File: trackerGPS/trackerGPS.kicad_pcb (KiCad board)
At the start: 4 copper layers, 89.4 x 33.6 mm, 47 parts, among them IC1 PIC32MM0256GPM028-I_ML, IC4 MAX17263LETD+, IC5 L86-M33, J1 USB_A, J2 Conn, J3 902-9235, Q1 BC847BW,115, Q2 BC847BW,115, U1 REG113NA-3.3_3K, U2 1043P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

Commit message: modified:   trackerGPS/microcontroller.bak 	modified:   trackerGPS/powerSupply.bak 	modified:   trackerGPS/powerSupply.sch 	modified:   trackerGPS/trackerGPS-cache.lib 	modified:   trackerGPS/trackerGPS.bak 	modified:   trackerGPS/trackerGPS.kicad_pcb 	modified:   trackerGPS/trackerGPS.kicad_pcb-bak
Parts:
- removed IC4: MAX17263LETD+, MAX17263LETD+:SON40P300X300X80-15N
- added IC2: BQ24072TRGTT, Package_DFN_QFN:QFN-16-1EP_3x3mm_P0.5mm_EP2.7x2.7mm_ThermalVias, F.Cu at (162.9, 91.8)
- added J4: USB_A, USB_JAE:DX4R005HJ5, F.Cu at (149.6, 106.9)
- moved C13 5.15 mm to (199.1, 34.8)
- moved C25 5.15 mm to (204.1, 40.9)
- moved C26 5.15 mm to (212.0, 39.7)
- moved IC1 5.15 mm to (206.2, 33.3)
- moved R7 5.15 mm to (196.6, 48.3)
- moved C10 5.15 mm to (213.2, 35.3)
- moved C12 5.15 mm to (211.1, 35.3)
- moved C22 5.15 mm to (208.3, 28.5)
- moved Q1 5.15 mm to (199.5, 47.8)
- moved Y1 5.15 mm to (208.1, 39.6)
- moved C14 5.15 mm to (201.1, 34.8)
- moved R6 5.15 mm to (199.6, 45.2)

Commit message: added battery charger BQ24072T 	modified:   trackerGPS/powerSupply.bak 	modified:   trackerGPS/powerSupply.sch 	modified:   trackerGPS/sym-lib-table 	modified:   trackerGPS/trackerGPS-cache.lib 	new file:   trackerGPS/trackerGPS-rescue.dcm 	new file:   trackerGPS/trackerGPS-rescue.lib 	modified:   trackerGPS/trackerGPS.kicad_pcb 	modified:   trackerGPS/trackerGPS.kicad_pcb-bak
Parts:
- removed U2: 1043P, 1043P:1043P
- added TP1: TestPoint, TestPoint:TestPoint_Pad_2.0x2.0mm, F.Cu at (181.5, 92.8)
- added TP2: TestPoint, TestPoint:TestPoint_Pad_2.0x2.0mm, F.Cu at (177.7, 92.8)

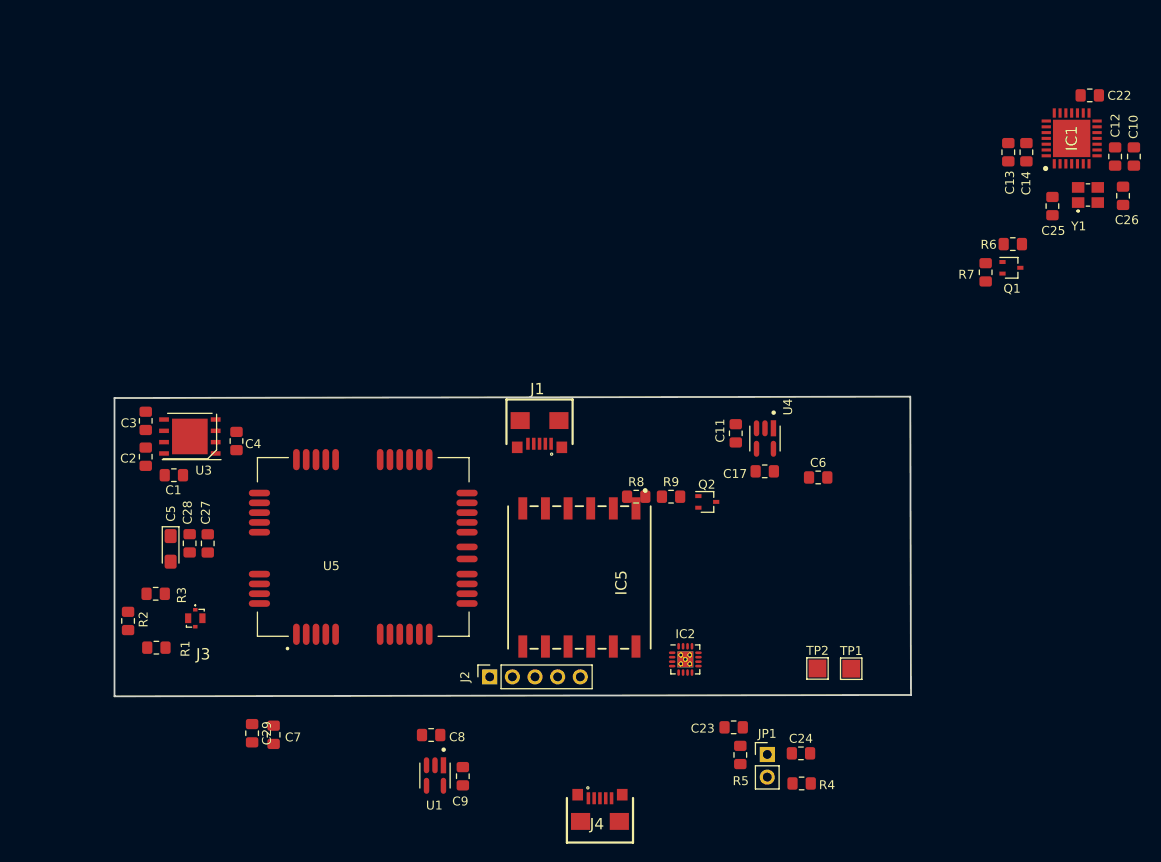
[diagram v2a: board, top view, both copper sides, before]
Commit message: Component placed 	modified:   trackerGPS/microcontroller.bak 	modified:   trackerGPS/microcontroller.sch 	modified:   trackerGPS/powerSupply.bak 	modified:   trackerGPS/powerSupply.sch 	modified:   trackerGPS/simModule.bak 	modified:   trackerGPS/simModule.sch 	modified:   trackerGPS/trackerGPS-cache.lib 	modified:   trackerGPS/trackerGPS.bak 	modified:   trackerGPS/trackerGPS.kicad_pcb 	modified:   trackerGPS/trackerGPS.kicad_pcb-bak 	modified:   trackerGPS/trackerGPS.sch
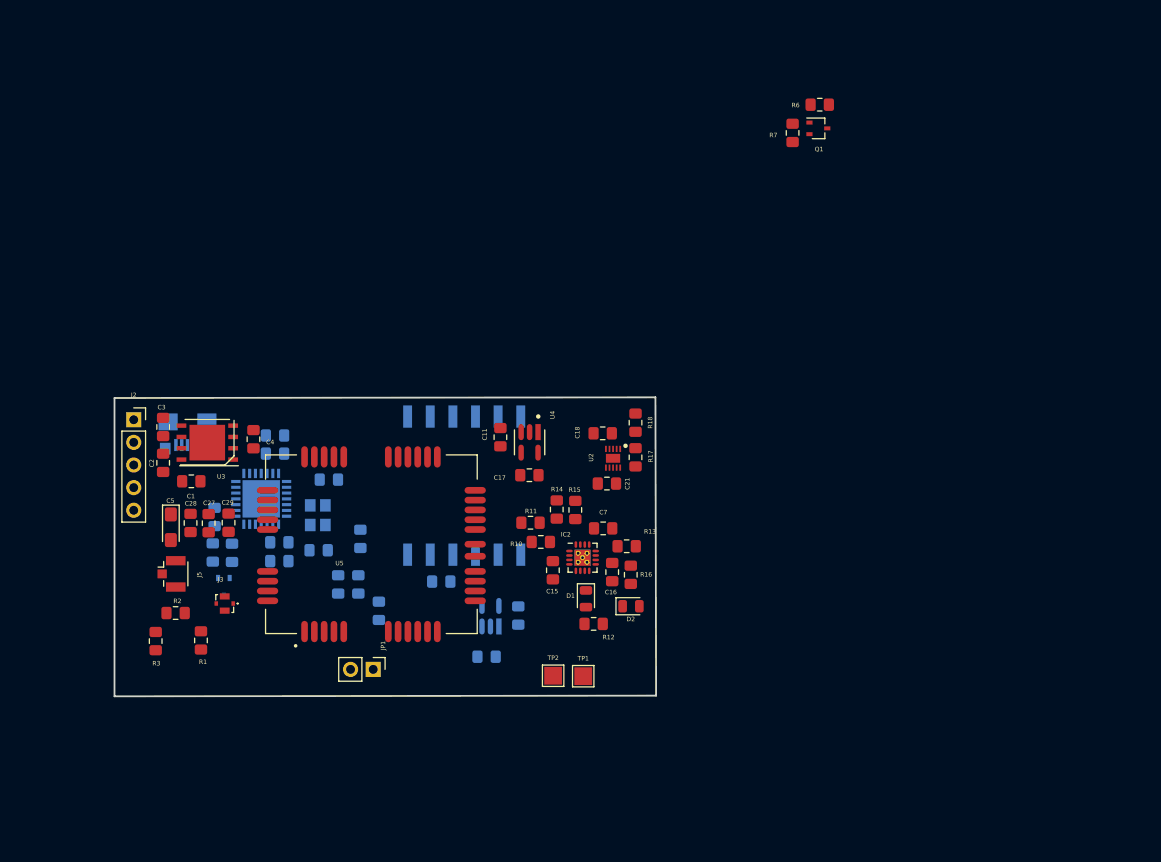
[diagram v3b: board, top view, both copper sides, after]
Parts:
- removed J1: USB_A, USB_JAE:DX4R005HJ5
- added C15: 4.7uF, Capacitor_SMD:C_0805_2012Metric_Pad1.15x1.40mm_HandSolder, F.Cu at (148.0, 81.8)
- added C16: 4.7uF, Capacitor_SMD:C_0805_2012Metric_Pad1.15x1.40mm_HandSolder, F.Cu at (154.7, 82.0)
- added C18: 470nF, Capacitor_SMD:C_0805_2012Metric_Pad1.15x1.40mm_HandSolder, F.Cu at (153.6, 66.4)
- added C21: 10uF, Capacitor_SMD:C_0805_2012Metric_Pad1.15x1.40mm_HandSolder, F.Cu at (154.1, 72.0)
- added D1: LED_Small, LED_SMD:LED_0805_2012Metric, F.Cu at (151.7, 85.0)
- added D2: LED_Small, LED_SMD:LED_0805_2012Metric, F.Cu at (156.8, 85.8)
- added J5: Conn_Coaxial, Connector_Coaxial:U.FL_Hirose_U.FL-R-SMT-1_Vertical, F.Cu at (105.2, 82.2)
- added R10: 200kOhm, Resistor_SMD:R_0805_2012Metric_Pad1.15x1.40mm_HandSolder, F.Cu at (146.7, 78.6)
- added R11: 49.9kOhm, Resistor_SMD:R_0805_2012Metric_Pad1.15x1.40mm_HandSolder, F.Cu at (145.5, 76.4)
- added R12: 1.5kOhm, Resistor_SMD:R_0805_2012Metric_Pad1.15x1.40mm_HandSolder, F.Cu at (152.6, 87.8)
- added R13: NP, Resistor_SMD:R_0805_2012Metric_Pad1.15x1.40mm_HandSolder, F.Cu at (156.3, 79.1)
- added R14: 900ohm, Resistor_SMD:R_0805_2012Metric_Pad1.15x1.40mm_HandSolder, F.Cu at (148.4, 74.9)
- added R15: 0ohm, Resistor_SMD:R_0805_2012Metric_Pad1.15x1.40mm_HandSolder, F.Cu at (150.5, 75.0)
- added R16: 1.5kOhm, Resistor_SMD:R_0805_2012Metric_Pad1.15x1.40mm_HandSolder, F.Cu at (156.7, 82.3)
- added R17: 5.56kOhm, Resistor_SMD:R_0805_2012Metric_Pad1.15x1.40mm_HandSolder, F.Cu at (157.3, 69.1)
- added R18: 1kOhm, Resistor_SMD:R_0805_2012Metric_Pad1.15x1.40mm_HandSolder, F.Cu at (157.3, 65.2)
- added U2: TLV75201PDSQT, TLV75201PDSQT:SON40P200X200X80-11N, F.Cu at (154.8, 69.2)
- C10, C12, C13, C14, C22, C23, C24, C25, C26, C6, C8, C9, IC1, IC5, J4, Q2, R4, R5, R8, R9, U1, Y1: moved to B.Cu
- C7: value C_Small -> 1uF
- TP1: value TestPoint -> Battery_GND
- TP2: value TestPoint -> Battery+
- moved C22 109.0 mm to (110.0, 75.8), turned to 270 degrees
- moved C10 106.1 mm to (117.3, 80.7), turned to 0 degrees
- moved C12 103.3 mm to (117.3, 78.6), turned to 0 degrees
- moved IC1 99.5 mm to (115.3, 73.8), turned to 180 degrees
- moved C26 98.6 mm to (121.7, 79.5), turned to 0 degrees
- moved Y1 93.6 mm to (121.6, 75.6), turned to 270 degrees
- moved C14 90.9 mm to (116.8, 68.7), turned to 0 degrees
- moved C13 88.2 mm to (116.8, 66.6), turned to 0 degrees
- moved C25 86.8 mm to (122.9, 71.6), turned to 0 degrees
- moved J4 60.4 mm to (103.3, 68.1)
- moved Q2 55.1 mm to (111.1, 83.6), turned to 270 degrees
- moved R4 54.5 mm to (126.2, 83.4), turned to 90 degrees
- moved R9 51.8 mm to (109.8, 79.8), turned to 90 degrees
- moved C24 50.0 mm to (128.5, 86.3), turned to 90 degrees
- moved J2 49.3 mm to (101.0, 64.9), turned to 0 degrees
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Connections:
- C10 pad 1: /powerSupply/Vcc_3.8V -> /powerSupply/Vcc_3.5V
- C11 pad 1: Net-(C11-Pad1) -> /microcontroller/VBUS
- C12 pad 1: /powerSupply/Vcc_3.8V -> /powerSupply/Vcc_3.5V
- C13 pad 1: /powerSupply/Vcc_3.8V -> /powerSupply/Vcc_3.5V
- C14 pad 1: /powerSupply/Vcc_3.8V -> /powerSupply/Vcc_3.5V
- C23 pad 1: /powerSupply/Vcc_3.8V -> /powerSupply/Vcc_3.5V
- C27 pad 1: /powerSupply/Vcc_3.8V -> /powerSupply/Vcc_3.5V
- C28 pad 1: /powerSupply/Vcc_3.8V -> /powerSupply/Vcc_3.5V
- C29 pad 1: /powerSupply/Vcc_3.8V -> /powerSupply/Vcc_3.5V
- C5 pad 1: /powerSupply/Vcc_3.8V -> /powerSupply/Vcc_3.5V
- C7 pad 1: /powerSupply/Vcc_3.8V -> /microcontroller/VBUS
- C8 pad 1: /powerSupply/Vcc_3.8V -> /powerSupply/3.8V_Bat_5V_USB
- IC1 pad 10: /powerSupply/Vcc_3.8V -> /powerSupply/Vcc_3.5V
- IC1 pad 12: Net-(C11-Pad1) -> /microcontroller/VBUS
- IC1 pad 18: /microcontroller/D- -> /microcontroller/USB-
- IC1 pad 19: /microcontroller/D+ -> /microcontroller/USB+
- IC1 pad 25: /powerSupply/Vcc_3.8V -> /powerSupply/Vcc_3.5V
- IC2 pad 10: Net-(IC2-Pad10) -> /powerSupply/3.8V_Bat_5V_USB
- IC2 pad 11: Net-(IC2-Pad11) -> /powerSupply/3.8V_Bat_5V_USB
- IC2 pad 13: Net-(IC2-Pad13) -> /microcontroller/VBUS
- IC2 pad 15: Net-(IC2-Pad15) -> GND
- IC2 pad 17: Net-(IC2-Pad17) -> GND
- IC2 pad 2: Net-(IC2-Pad2) -> Net-(C15-Pad1)
- IC2 pad 3: Net-(IC2-Pad3) -> Net-(C15-Pad1)
- IC2 pad 4: Net-(IC2-Pad4) -> GND
- IC2 pad 5: Net-(IC2-Pad5) -> GND
- IC2 pad 6: Net-(IC2-Pad6) -> GND
- IC2 pad 8: Net-(IC2-Pad8) -> GND
- J2 pad 4: /powerSupply/Vcc_3.8V -> /powerSupply/Vcc_3.5V
- J4 pad 1: Net-(J4-Pad1) -> /microcontroller/VBUS
- J4 pad 2: Net-(J4-Pad2) -> /microcontroller/USB-
- J4 pad 3: Net-(J4-Pad3) -> /microcontroller/USB+
- J4 pad 4: Net-(J4-Pad4) -> GND
- J4 pad 5: Net-(J4-Pad5) -> GND
- R5 pad 2: /powerSupply/Vcc_3.8V -> /powerSupply/Vcc_3.5V
- TP2 pad 1: /powerSupply/Vcc_3.8V -> Net-(C15-Pad1)
- U1 pad 1: /powerSupply/Vcc_3.8V -> /powerSupply/3.8V_Bat_5V_USB
- U4 pad 1: Net-(C11-Pad1) -> /microcontroller/VBUS
- U4 pad 3: Net-(C11-Pad1) -> /microcontroller/VBUS
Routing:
- added copper zone on In1.Cu, net GND
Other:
- board size 89.4 x 33.6 mm -> 60.8 x 33.6 mm

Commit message: PCB completed with test points 	modified:   trackerGPS/gpsModule.bak 	modified:   trackerGPS/gpsModule.sch 	modified:   trackerGPS/microcontroller.bak 	modified:   trackerGPS/microcontroller.sch 	modified:   trackerGPS/powerSupply.bak 	modified:   trackerGPS/powerSupply.sch 	modified:   trackerGPS/simModule.bak 	modified:   trackerGPS/simModule.sch 	modified:   trackerGPS/trackerGPS-cache.lib 	modified:   trackerGPS/trackerGPS.bak 	modified:   trackerGPS/trackerGPS.kicad_pcb 	modified:   trackerGPS/trackerGPS.kicad_pcb-bak 	modified:   trackerGPS/trackerGPS.sch
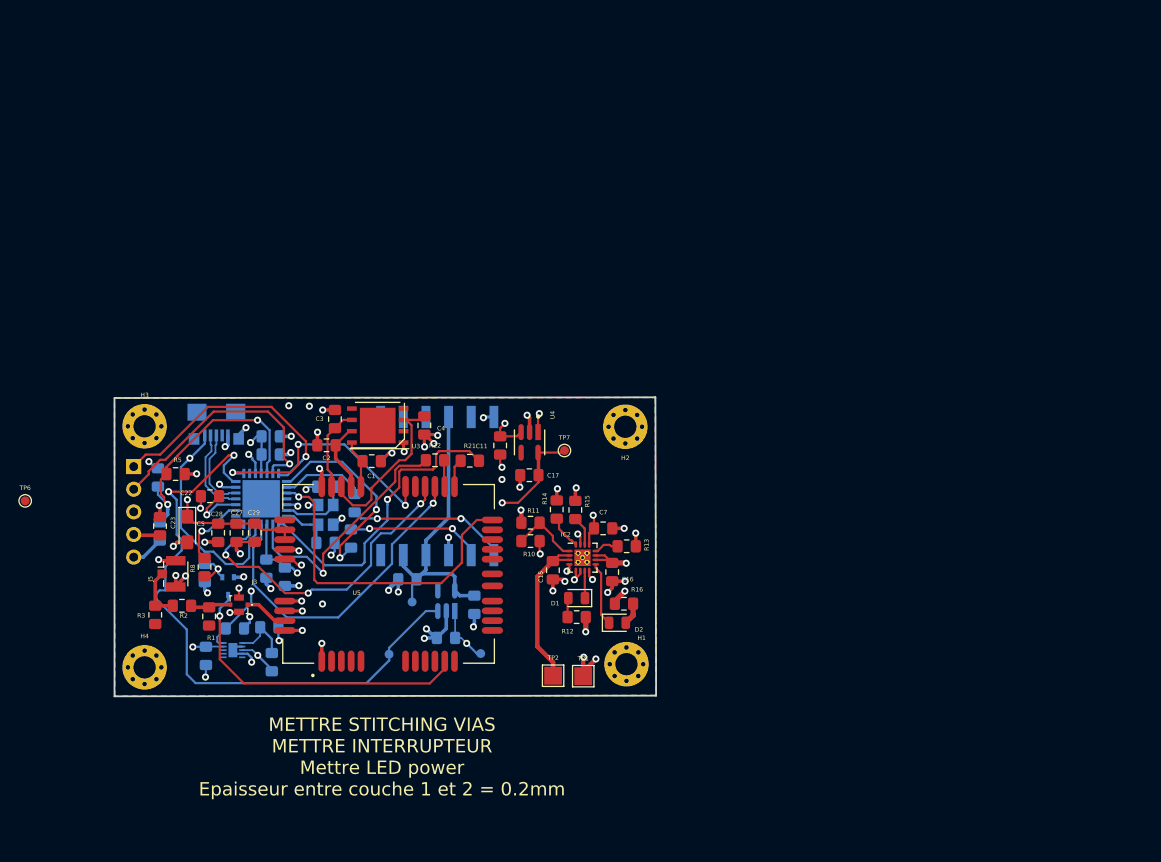
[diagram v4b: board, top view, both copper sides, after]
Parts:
- removed JP1: Jumper, Connector_PinHeader_2.54mm:PinHeader_1x02_P2.54mm_Vertical
- removed Q1: BC847BW,115, Package_TO_SOT_SMD:SOT-323_SC-70
- removed R6: 10kOhm, Resistor_SMD:R_0805_2012Metric_Pad1.15x1.40mm_HandSolder
- removed R7: 47kOhm, Resistor_SMD:R_0805_2012Metric_Pad1.15x1.40mm_HandSolder
- added H1: MountingHole_Pad, MountingHole:MountingHole_2.5mm_Pad_Via, F.Cu at (156.3, 92.3)
- added H2: MountingHole_Pad, MountingHole:MountingHole_2.5mm_Pad_Via, F.Cu at (156.1, 65.7)
- added H3: MountingHole_Pad, MountingHole:MountingHole_2.5mm_Pad_Via, F.Cu at (102.2, 65.6)
- added H4: MountingHole_Pad, MountingHole:MountingHole_2.5mm_Pad_Via, F.Cu at (102.2, 92.7)
- added R19: 0ohm, Resistor_SMD:R_0805_2012Metric_Pad1.15x1.40mm_HandSolder, B.Cu at (125.3, 78.2)
- added R20: 0ohm, Resistor_SMD:R_0805_2012Metric_Pad1.15x1.40mm_HandSolder, B.Cu at (125.8, 74.2)
- added R21: 0ohm, Resistor_SMD:R_0805_2012Metric_Pad1.15x1.40mm_HandSolder, F.Cu at (138.7, 69.5)
- added R22: 0ohm, Resistor_SMD:R_0805_2012Metric_Pad1.15x1.40mm_HandSolder, F.Cu at (134.8, 69.4)
- added TP3: LDO_ENABLE, TestPoint:TestPoint_Pad_D1.0mm, B.Cu at (129.6, 91.2)
- added TP4: TP_chg, TestPoint:TestPoint_Pad_D1.0mm, B.Cu at (139.9, 91.1)
- added TP5: TP_3v3_GPS, TestPoint:TestPoint_Pad_D1.0mm, B.Cu at (132.2, 85.3)
- added TP6: REF_CLK, TestPoint:TestPoint_Pad_D1.0mm, F.Cu at (88.8, 74.0)
- added TP7: VUSB3V3, TestPoint:TestPoint_Pad_D1.0mm, F.Cu at (149.3, 68.3)
- C18, C21, J2, R17, R18, U2: moved to B.Cu
- C22, C23, R8: moved to F.Cu
- J4: value USB_A -> USB_B_Micro
- R4: value 10kOhm -> 602ohm
- R5: value 602kOhm -> 10kOhm; moved to F.Cu
- moved C21 49.0 mm to (109.1, 91.4), turned to 270 degrees
- moved U2 47.8 mm to (112.1, 90.7), turned to 180 degrees
- moved R18 47.1 mm to (116.2, 88.2), turned to 180 degrees
- moved R17 46.8 mm to (116.5, 92.1)
- moved C18 46.7 mm to (112.3, 88.3), turned to 0 degrees
- moved C24 29.0 mm to (103.7, 71.3)
- moved R4 23.1 mm to (103.9, 77.4), turned to 270 degrees
- moved C23 22.5 mm to (103.9, 76.8)
- moved R5 22.1 mm to (105.7, 71.0), turned to 0 degrees
- moved C1 20.4 mm to (127.7, 69.5)
- moved C3 19.3 mm to (123.5, 64.8)
- moved C4 19.2 mm to (133.6, 65.5)
- moved U3 19.2 mm to (128.3, 65.5)
- moved C2 18.4 mm to (122.6, 67.7), turned to 180 degrees
- moved J2 5.26 mm to (101.0, 70.1), turned to 180 degrees
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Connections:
- net /powerSupply/3.8V_Bat_5V_USB renamed /powerSupply/3.8V_Bat_OR_5V_USB
- net Net-(C17-Pad1) renamed /microcontroller/VUSB3V3
- IC1 pad 2: /gpsModule/UART_RX_GSM -> /microcontroller/UART_TX2_UC
- IC1 pad 21: Net-(IC1-Pad21) -> /microcontroller/LDO_ENABLE
- IC1 pad 23: /microcontroller/LDO_ENABLE -> Net-(IC1-Pad23)
- IC1 pad 26: Net-(IC1-Pad26) -> Net-(C24-Pad1)
- IC1 pad 8: /simModule/UART_RX_GSM -> /microcontroller/UART_TX3_UC
- IC5 pad 12: Net-(IC5-Pad12) -> GND
- IC5 pad 2: /microcontroller/UART_RX2_UC -> /gpsModule/UART_TX_GSM
- IC5 pad 3: Net-(IC5-Pad3) -> GND
- J4 pad 4: GND -> Net-(J4-Pad4)
- J4 pad 6: (no net) -> GND
- R4 pad 1: Net-(IC1-Pad26) -> Net-(C24-Pad1)
- R5 pad 1: Net-(IC1-Pad26) -> Net-(C24-Pad1)
- U5 pad 22: /microcontroller/UART_RX3_UC -> /simModule/UART_TX_GSM
- U5 pad 23: /simModule/UART_GSM_RTS -> /microcontroller/UART_CTS3_UC
- U5 pad 24: /microcontroller/UART_CTS3_UC -> /simModule/UART_GSM_RTS
- U5 pad 33: Net-(FB1-Pad1) -> /powerSupply/Vcc_3.5V
- U5 pad 34: Net-(FB1-Pad1) -> /powerSupply/Vcc_3.5V
- Y1 pad 2: Net-(Y1-Pad2) -> GND
- Y1 pad 4: Net-(Y1-Pad4) -> GND
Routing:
- net GND: track 0.00 -> 112.8 mm, vias 0 -> 70
- net /microcontroller/VBUS: track 0.00 -> 75.6 mm, vias 0 -> 6
- net /microcontroller/LDO_ENABLE: track 0.00 -> 70.5 mm, vias 0 -> 2
- net /powerSupply/Vcc_3.5V: track 0.00 -> 68.0 mm, vias 0 -> 7
- net /microcontroller/VUSB3V3: track 0.00 -> 46.0 mm, vias 0 -> 2
- net /microcontroller/UART_CTS3_UC: track 0.00 -> 37.4 mm, vias 0 -> 1
- net /microcontroller/SLEEP: track 0.00 -> 37.1 mm, vias 0 -> 1
- net /simModule/UART_GSM_RTS: track 0.00 -> 36.5 mm, vias 0 -> 3
- net /simModule/GSM_POWER_ON: track 0.00 -> 35.5 mm, vias 0 -> 1
- net /microcontroller/UART_TX3_UC: track 0.00 -> 34.6 mm, vias 0 -> 1
- net /powerSupply/Vcc_3.3V: track 0.00 -> 34.5 mm
- net Net-(IC1-Pad28): track 0.00 -> 29.4 mm, vias 0 -> 1
- net Net-(C24-Pad1): track 0.00 -> 28.8 mm, vias 0 -> 2
- net Net-(IC1-Pad27): track 0.00 -> 28.5 mm, vias 0 -> 1
- net /microcontroller/UART_RX3_UC: track 0.00 -> 28.3 mm, vias 0 -> 1
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- added copper zone on In2.Cu, net /microcontroller/VBUS
- added copper zone on In2.Cu, net /powerSupply/3.8V_Bat_OR_5V_USB
- added copper zone on In2.Cu, net /powerSupply/Vcc_3.5V
- added copper zone on B.Cu, net GND
- added copper zone on F.Cu, net GND
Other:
- net class Default: clearance 0.2 -> 0.1
- rule trace_clearance: 0.2 -> 0.1
- board text added: "Emplacement Batterie"
- board text added: "METTRE STITCHING VIAS METTRE INTERRUPTEUR Mettre LED power Epaisseur entre couche 1 et 2 = 0.2mm"

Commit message: Replaced TLV75201 by REG113NA 	modified:   "Bilan energ\303\251tique tracker GPS.xlsx" 	modified:   trackerGPS/microcontroller.bak 	modified:   trackerGPS/powerSupply.bak 	modified:   trackerGPS/powerSupply.sch 	modified:   trackerGPS/trackerGPS-cache.lib 	modified:   trackerGPS/trackerGPS.bak 	modified:   trackerGPS/trackerGPS.kicad_pcb 	modified:   trackerGPS/trackerGPS.kicad_pcb-bak 	modified:   trackerGPS/trackerGPS.sch
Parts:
- removed C21: 10uF, Capacitor_SMD:C_0805_2012Metric_Pad1.15x1.40mm_HandSolder
- removed R17: 5.56kOhm, Resistor_SMD:R_0805_2012Metric_Pad1.15x1.40mm_HandSolder
- removed R18: 1kOhm, Resistor_SMD:R_0805_2012Metric_Pad1.15x1.40mm_HandSolder
- added C19: 4.7uF, Capacitor_SMD:C_0805_2012Metric_Pad1.15x1.40mm_HandSolder, B.Cu at (108.7, 91.8)
- added R6: 0Ohm, Resistor_SMD:R_0805_2012Metric_Pad1.15x1.40mm_HandSolder, B.Cu at (129.8, 88.1)
- added TP8: GND, TestPoint:TestPoint_Pad_D1.0mm, B.Cu at (125.1, 88.3)
- C18: value 470nF -> 4.7uF
- U2: value TLV75201PDSQT -> REG113NA-3.3_3K; footprint TLV75201PDSQT:SON40P200X200X80-11N -> REG113NA:Texas_Instruments-DBV0005A-0-0-IPC_A
- moved TP6 27.6 mm to (115.8, 68.4)
- moved U2 1.58 mm to (112.4, 92.3)
- moved C18 0.69 mm to (112.4, 89.0), turned to 180 degrees
- moved TP4 0.60 mm to (139.5, 90.7)
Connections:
- net /powerSupply/Vcc_3.3V renamed /powerSupply/Vcc_3.3V_GPS
- C10 pad 1: /powerSupply/Vcc_3.5V -> /powerSupply/Vcc_3.3V_UC
- C12 pad 1: /powerSupply/Vcc_3.5V -> /powerSupply/Vcc_3.3V_UC
- C13 pad 1: /powerSupply/Vcc_3.5V -> /powerSupply/Vcc_3.3V_UC
- C14 pad 1: /powerSupply/Vcc_3.5V -> /powerSupply/Vcc_3.3V_UC
- C16 pad 1: /powerSupply/3.8V_Bat_OR_5V_USB -> /powerSupply/Vcc_BAT_GSM
- C18 pad 1: /powerSupply/Vcc_3.5V -> /powerSupply/Vcc_BAT_GSM
- C23 pad 1: /powerSupply/Vcc_3.5V -> /powerSupply/Vcc_3.3V_UC
- C27 pad 1: /powerSupply/Vcc_3.5V -> /powerSupply/Vcc_BAT_GSM
- C28 pad 1: /powerSupply/Vcc_3.5V -> /powerSupply/Vcc_BAT_GSM
- C29 pad 1: /powerSupply/Vcc_3.5V -> /powerSupply/Vcc_BAT_GSM
- C5 pad 1: /powerSupply/Vcc_3.5V -> /powerSupply/Vcc_BAT_GSM
- C8 pad 1: /powerSupply/3.8V_Bat_OR_5V_USB -> /powerSupply/Vcc_BAT_GSM
- IC1 pad 10: /powerSupply/Vcc_3.5V -> /powerSupply/Vcc_3.3V_UC
- IC1 pad 25: /powerSupply/Vcc_3.5V -> /powerSupply/Vcc_3.3V_UC
- IC2 pad 10: /powerSupply/3.8V_Bat_OR_5V_USB -> /powerSupply/Vcc_BAT_GSM
- IC2 pad 11: /powerSupply/3.8V_Bat_OR_5V_USB -> /powerSupply/Vcc_BAT_GSM
- J2 pad 4: /powerSupply/Vcc_3.5V -> /powerSupply/Vcc_3.3V_UC
- R12 pad 2: /powerSupply/3.8V_Bat_OR_5V_USB -> /powerSupply/Vcc_BAT_GSM
- R16 pad 2: /powerSupply/3.8V_Bat_OR_5V_USB -> /powerSupply/Vcc_BAT_GSM
- R5 pad 2: /powerSupply/Vcc_3.5V -> /powerSupply/Vcc_3.3V_UC
- TP4 pad 1: /powerSupply/3.8V_Bat_OR_5V_USB -> /powerSupply/Vcc_BAT_GSM
- U1 pad 1: /powerSupply/3.8V_Bat_OR_5V_USB -> /powerSupply/Vcc_BAT_GSM
- U2 pad 1: Net-(R17-Pad1) -> /powerSupply/Vcc_BAT_GSM
- U2 pad 3: /powerSupply/Vcc_3.5V -> /powerSupply/Vcc_BAT_GSM
- U2 pad 4: GND -> Net-(U2-Pad4)
- U2 pad 5: Net-(U2-Pad5) -> /powerSupply/Vcc_3.3V_UC
- U5 pad 33: /powerSupply/Vcc_3.5V -> /powerSupply/Vcc_BAT_GSM
- U5 pad 34: /powerSupply/Vcc_3.5V -> /powerSupply/Vcc_BAT_GSM
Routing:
- net /powerSupply/Vcc_3.5V: track 68.0 -> 0.00 mm, vias 7 -> 0
- net /powerSupply/Vcc_3.3V_UC: track 0.00 -> 56.0 mm, vias 0 -> 6
- net /powerSupply/Vcc_BAT_GSM: track 0.00 -> 40.2 mm, vias 0 -> 8
- net /powerSupply/3.8V_Bat_OR_5V_USB: track 19.4 -> 0.00 mm, vias 5 -> 0
- net Net-(R17-Pad1): track 6.74 -> 0.00 mm
- net Net-(IC1-Pad23): track 0.00 -> 6.04 mm, vias 0 -> 1
- net GND: track 112.8 -> 109.2 mm, vias 70 -> 67
- net /simModule/GSM_POWER_ON: track 35.5 -> 38.1 mm
- net /microcontroller/LDO_ENABLE: track 70.5 -> 68.5 mm
- net Net-(C24-Pad1): track 28.8 -> 27.8 mm
- net Net-(J3-Pad2): track 4.62 -> 5.19 mm
- added copper zone on In2.Cu, net /powerSupply/Vcc_3.3V_UC
- added copper zone on In2.Cu, net /powerSupply/Vcc_BAT_GSM
- removed copper zone on In2.Cu, net /powerSupply/3.8V_Bat_OR_5V_USB
- removed copper zone on In2.Cu, net /powerSupply/Vcc_3.5V
